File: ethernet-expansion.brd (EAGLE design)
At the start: 64.4 x 38.1 mm, 21 parts, among them Q1 25MHz, U1 ENC28J60-SO

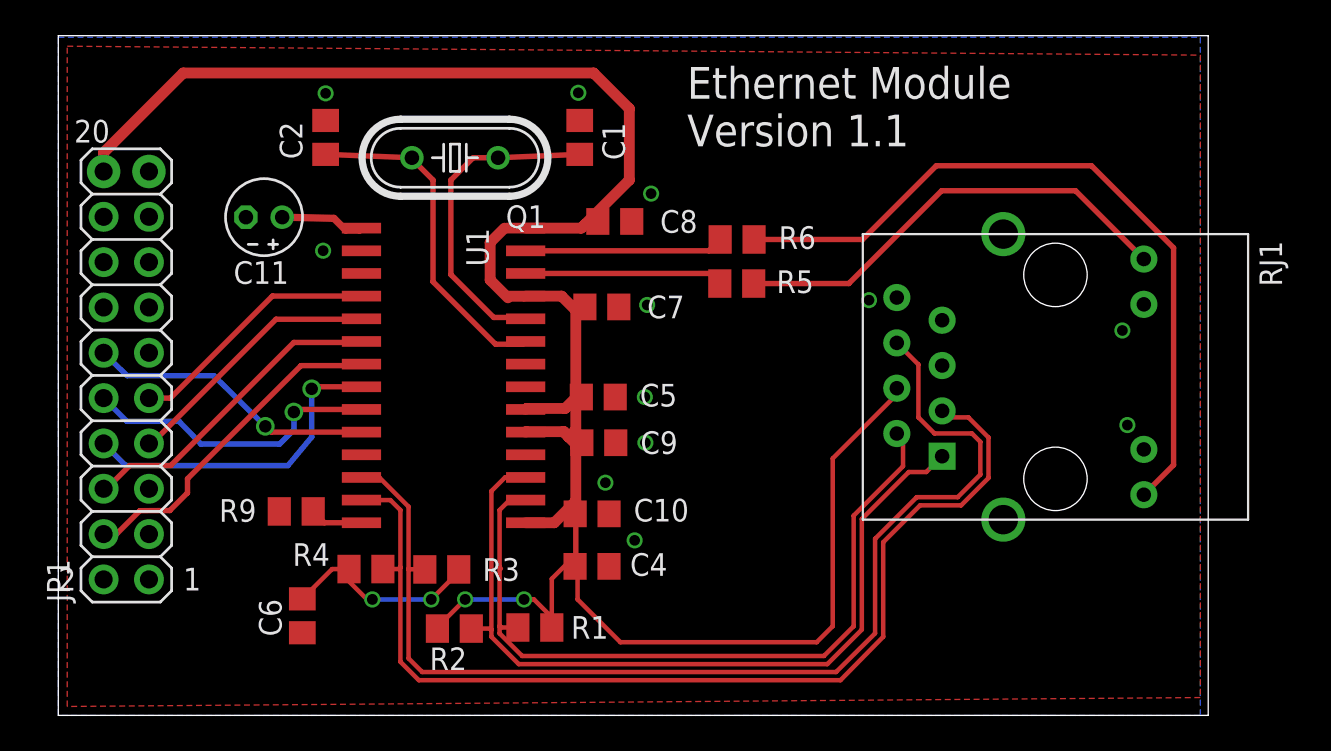
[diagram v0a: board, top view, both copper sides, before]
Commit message: Swapping header pin rows to make it correct, and adding debug uart pins
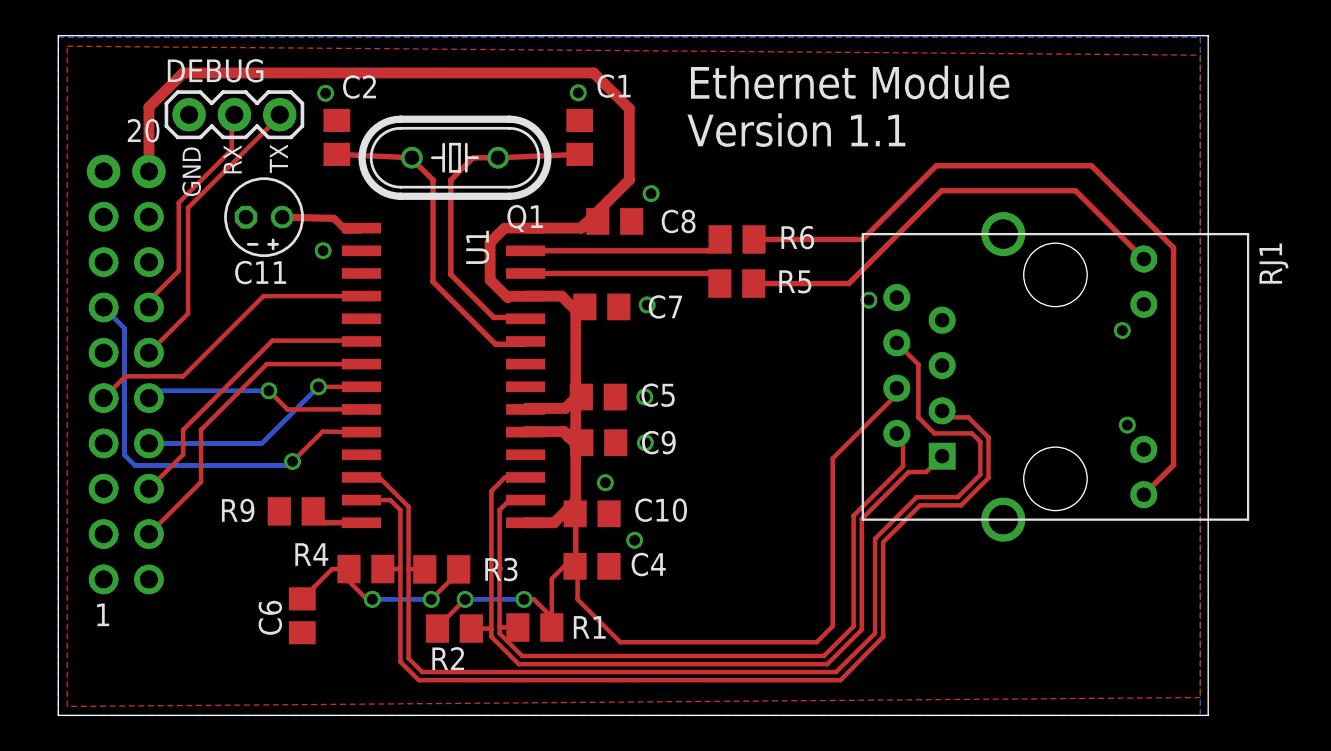
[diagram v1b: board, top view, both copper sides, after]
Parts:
- added DEBUG: (no value), SparkFun-Connectors:1X03
- moved C2 0.63 mm to (15.6, 32.4)
- flipped JP1 to the bottom
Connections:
- net ETH_INT0 renamed ETH_INT
- removed net ETH_INT1: JP1.7, U1.5
- new net RX: DEBUG.2, JP1.14
- new net TX: DEBUG.3, JP1.12
- net ETH_RESET: now also JP1.13; no longer JP1.12
- net GND: now also DEBUG.1
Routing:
- net TX: track 0.00 -> 16.4 mm
- net ETH_INT1: track 14.8 -> 0.00 mm
- net RX: track 0.00 -> 12.8 mm
- net ETH_RESET: track 16.3 -> 23.1 mm
- net ETH_CLK: track 18.5 -> 13.2 mm
- net ETH_CS: track 16.9 -> 12.5 mm
- net ETH_INT: track 14.3 -> 16.8 mm
- net ETH_MISO: track 17.9 -> 16.2 mm
- net ETH_MOSI: track 18.8 -> 17.6 mm
- net +3V3: track 124.8 -> 123.8 mm
- net N$12: track 19.0 -> 18.4 mm
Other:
- board text added: "GND"
- board text added: "RX"
- board text added: "TX"
- board text removed: "2"
